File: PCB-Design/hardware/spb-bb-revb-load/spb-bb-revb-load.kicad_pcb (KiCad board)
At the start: 4 copper layers, 89.5 x 80 mm, 200 parts, among them J1 DC+, J10 U.FL L2, J11 U.FL D2, J12 V_ISO,HS in: 1 +, 2 -, J13 V_ISO,LS in: 1 +, 2 -, J14 CTRL2: 1 12V 2 GND 3 PWM_H 4 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, J15 FAN 12V: 1 +12V, 2 GND, J16 U.FL H3, J17 U.FL L3, J18 U.FL D3, J19 U.FL H4, J2 DC-, J20 U.FL L4, J21 U.FL D4, J22 AC, J23 1:NTC 2:DC- (LS domain!), J3 V_ISO,HS in: 1 +, 2 -, J4 V_ISO,LS in: 1 +, 2 -, J5 CTRL1: 1 12V 2 GND 3 PWM_H 4 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, J6 U.FL H1, J7 U.FL L1, J8 U.FL D1, J9 U.FL H2, Q1 EPC2361, Q2 EPC2361, Q3 EPC2361, Q4 EPC2361, Q5 EPC2361, Q6 EPC2361, Q7 EPC2361, Q8 EPC2361, U1 2EDF7275K, U2 2EDF7275K

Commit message: Rev B boards: full silkscreen; Q3D fast set fixed (R-only DC, bank model)
- silk_placer.py: collision-checked placement (pads, silk, outline) of every reference
  (connectors with their function, U.FL with the measured signal), connector pin names, DC+/DC-,
  AC, cell numbers, polarity warning, board name; DRC 0/0/0 on both boards; fab files regenerated
- Q3D: DC solved for R only (the DC-inductance pass hung > 19 h), new bank crop (terminals +
  bank + bypass, AC 1 MHz) for the leg DC-link port and L_b; final_post after every step

Co-Authored-By: Claude Opus 5.5 <noreply@anthropic.com>
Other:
- board text added: "+"
- board text added: "+12V"
- board text added: "-"
- board text added: "12V"
- board text added: "2"
- board text added: "3"
- board text added: "75 V DC - CHECK POLARITY"
- board text added: "AC"
- board text added: "C1"
- board text added: "C10"
- board text added: "C11"
- board text added: "C12"
- board text added: "C13"
- board text added: "C14"
- board text added: "C15"
- board text added: "C16"
- board text added: "C17"
- board text added: "C18"
- board text added: "C19"
- board text added: "C2"
- board text added: "C20"
- board text added: "C21"
- board text added: "C22"
- board text added: "C23"
- board text added: "C24"
- board text added: "C25"
- board text added: "C26"
- board text added: "C27"
- board text added: "C28"
- board text added: "C29"
- board text added: "C3"
- board text added: "C30"
- board text added: "C31"
- board text added: "C32"
- board text added: "C33"
- board text added: "C34"
- board text added: "C35"
- board text added: "C36"
- board text added: "C37"
- board text added: "C38"
- board text added: "C39"
- board text added: "C4"
- board text added: "C40"
- board text added: "C41"
- board text added: "C42"
- board text added: "C43"
- board text added: "C44"
- board text added: "C45"
- board text added: "C46"
- board text added: "C47"
- board text added: "C48"
- board text added: "C49"
- board text added: "C5"
- board text added: "C50"
- board text added: "C51"
- board text added: "C52"
- board text added: "C53"
- board text added: "C54"
- board text added: "C55"
- board text added: "C56"
- board text added: "C57"
- board text added: "C58"
- board text added: "C59"
- board text added: "C6"
- board text added: "C60"
- board text added: "C61"
- board text added: "C62"
- board text added: "C63"
- board text added: "C64"
- board text added: "C65"
- board text added: "C66"
- board text added: "C67"
- board text added: "C68"
- board text added: "C69"
- board text added: "C7"
- board text added: "C70"
- board text added: "C71"
- board text added: "C72"
- board text added: "C73"
- board text added: "C74"
- board text added: "C75"
- board text added: "C76"
- board text added: "C77"
- board text added: "C78"
- board text added: "C79"
- board text added: "C8"
- board text added: "C80"
- board text added: "C81"
- board text added: "C82"
- board text added: "C83"
- board text added: "C84"
- board text added: "C85"
- board text added: "C86"
- board text added: "C87"
- board text added: "C88"
- board text added: "C9"
- board text added: "CELL 1"
- board text added: "CELL 4"
- board text added: "D1"
- board text added: "D10 HV"
- board text added: "D2"
- board text added: "D3"
- board text added: "D4"
- board text added: "D5 12V"
- board text added: "D6"
- board text added: "D7"
- board text added: "D8"
- board text added: "D9"
- board text added: "DIS"
- board text added: "GND"
- board text added: "J1 DC+"
- board text added: "J10 VGS-L2"
- board text added: "J11 VDS-L2"
- board text added: "J12 HS-ISO"
- board text added: "J13 LS-ISO"
- board text added: "J14 CTRL2"
- board text added: "J15 FAN"
- board text added: "J16 VGS-H3"
- board text added: "J17 VGS-L3"
- board text added: "J18 VDS-L3"
- board text added: "J19 VGS-H4"
- board text added: "J2 DC-"
- board text added: "J20 VGS-L4"
- board text added: "J21 VDS-L4"
- board text added: "J22 AC"
- board text added: "J23 NTC"
- board text added: "J3 HS-ISO"
- board text added: "J4 LS-ISO"
- board text added: "J5 CTRL1"
- board text added: "J6 VGS-H1"
- board text added: "J7 VGS-L1"
- board text added: "J8 VDS-L1"
- board text added: "J9 VGS-H2"
- board text added: "KTH 2026-10 4 x EPC2361 PER SWITCH"
- board text added: "L1"
- board text added: "L10"
- board text added: "L2"
- board text added: "L3"
- board text added: "L4"
- board text added: "L5"
- board text added: "L6"
- board text added: "L7"
- board text added: "L8"
- board text added: "L9"
- board text added: "NTC"
- board text added: "PWMH"
- board text added: "PWML"
- board text added: "Q1"
- board text added: "Q2"
- board text added: "Q3"
- board text added: "Q4"
- board text added: "Q5"
- board text added: "Q6"
- board text added: "Q7"
- board text added: "Q8"
- board text added: "R1"
- board text added: "R10"
- board text added: "R11"
- board text added: "R12"
- board text added: "R13"
- board text added: "R14"
- board text added: "R15"
- board text added: "R16"
- board text added: "R17"
- board text added: "R18"
- board text added: "R19"
- board text added: "R2"
- board text added: "R20"
- board text added: "R21"
- board text added: "R22"
- board text added: "R23"
- board text added: "R24"
- board text added: "R25"
- board text added: "R26"
- board text added: "R27"
- board text added: "R28"
- board text added: "R29"
- board text added: "R3"
- board text added: "R30"
- board text added: "R31"
- board text added: "R32"
- board text added: "R33"
- board text added: "R34"
- board text added: "R35"
- board text added: "R36"
- board text added: "R37"
- board text added: "R38"
- board text added: "R39"
- board text added: "R4"
- board text added: "R40"
- board text added: "R41"
- board text added: "R42"
- board text added: "R43"
- board text added: "R44"
- board text added: "R45"
- board text added: "R46"
- board text added: "R47"
- board text added: "R48"
- board text added: "R49"
- board text added: "R5"
- board text added: "R50"
- board text added: "R6"
- board text added: "R7"
- board text added: "R8"
- board text added: "R9"
- board text added: "RT1"
- board text added: "SPB LEG REV B - LOAD-TEST BOARD"
- board text added: "U1"
- board text added: "U2"
- board text removed: "HV"

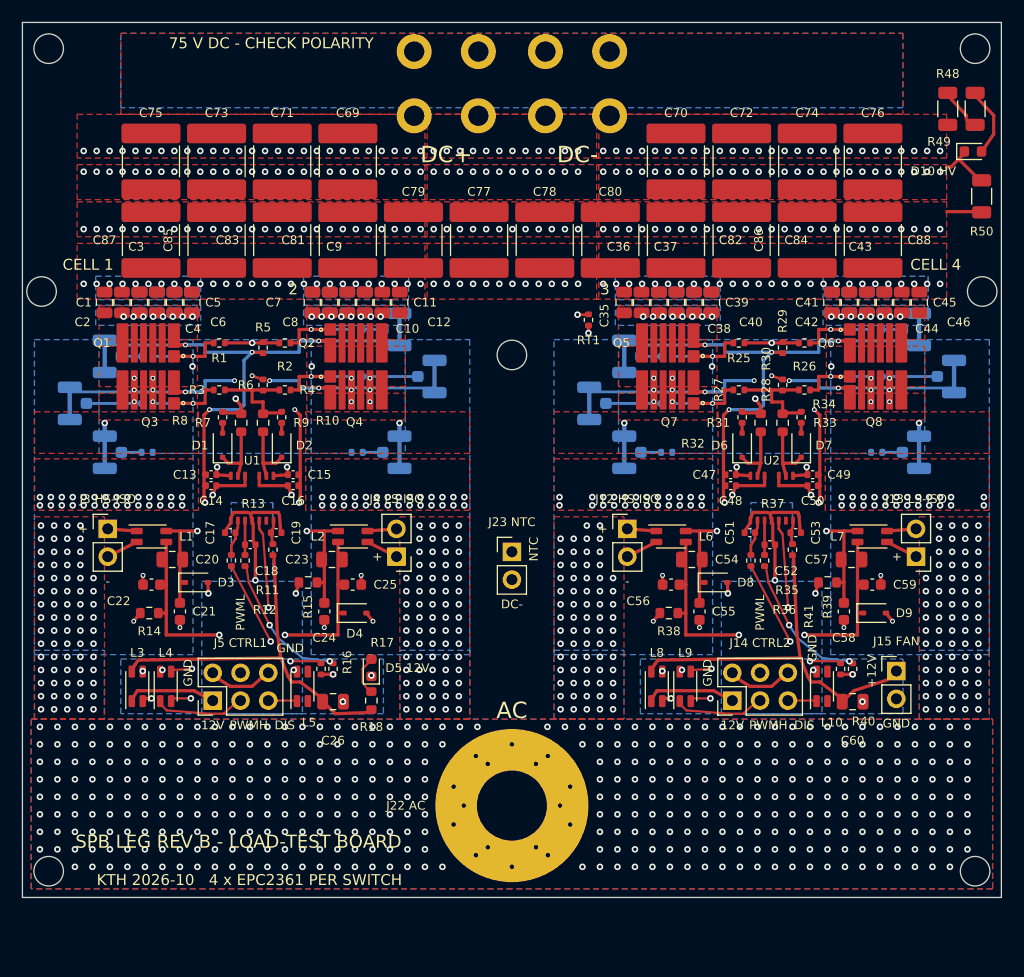
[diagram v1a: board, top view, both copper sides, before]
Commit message: Rev B boards: 1200 V control/power barrier and per-pair common-mode filtering
- Rule set in <board>.kicad_dru (exact net lists): control vs power 4.0 mm on the outer
  layers (IPC-2221B B4/A6), 3.0 mm inner (B1), 3.0 mm inside the 2EDF7275K courtyard,
  0.2 mm between the 75 V power domains. DRC 0/0 on both boards, schematic = PCB.
- Control area per block: top-layer SMD only (+ bottom GNDI plane), 4 mm / 3 mm barrier
  keepouts, nothing under the chokes and the connector on any layer.
- 2x5 SMT control header with a return next to every signal (PWM_H, PWM_L, DIS, 12 V,
  NTC), one WE-CNSW choke per pair, 12 V ferrite bead; NTC moved to the control side.
- Gate-supply islands moved outside the barrier, supplies routed on L3 around it,
  output decoupling on the bottom; AC bus/bolt 5.2 mm lower (board 89.5 x 85.2 mm).
- Removed: DC- referenced NTC header, 12 V LED, fan header (fan from the bench).
- Fab notes: IPC class 2, solder mask over all copper, all vias tented.

Co-Authored-By: Claude Opus 5.5 <noreply@anthropic.com>
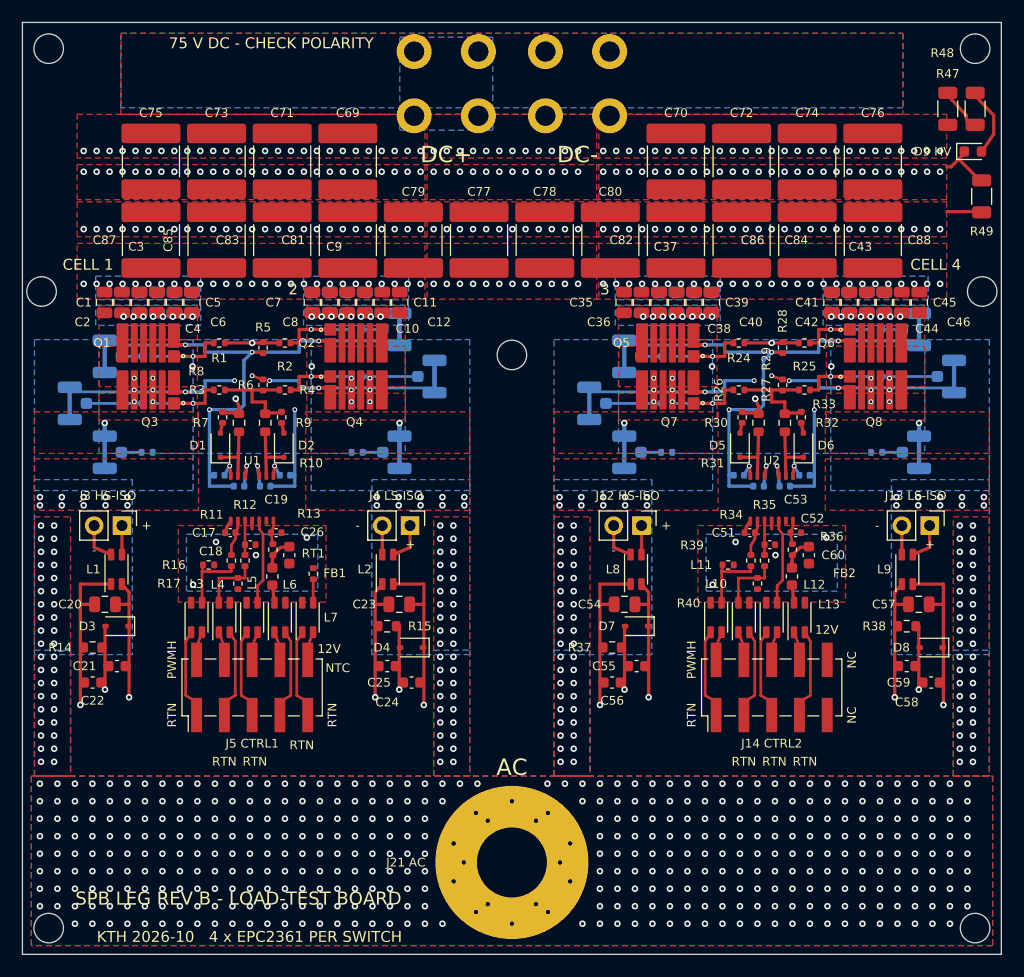
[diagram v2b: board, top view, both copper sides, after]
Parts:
- removed D10: red 0603 (DC link present), LED_SMD:LED_0603_1608Metric
- removed J22: AC, spb_fab:AC_BOLT_M6
- removed J23: 1:NTC 2:DC- (LS domain!), Connector_PinHeader_2.54mm:PinHeader_1x02_P2.54mm_Vertical
- removed R50: 100k 1206 (bleeder), Resistor_SMD:R_1206_3216Metric
- added FB1: BLM18PG221SN1 (220 R @ 100 MHz), Inductor_SMD:L_0603_1608Metric, F.Cu at (128.1, 126.2)
- added FB2: BLM18PG221SN1 (220 R @ 100 MHz), Inductor_SMD:L_0603_1608Metric, F.Cu at (175.6, 126.2)
- added L11: WE-CNSW 744232601, spb_fab:L_CommonMode_Wurth_WE-CNSW-1206, F.Cu at (171.2, 130.0)
- added L12: WE-CNSW 744232601, spb_fab:L_CommonMode_Wurth_WE-CNSW-1206, F.Cu at (173.8, 130.0)
- added L13: WE-CNSW 744232601, spb_fab:L_CommonMode_Wurth_WE-CNSW-1206, F.Cu at (176.3, 130.0)
- C13, C14, C15, C16, C47, C48, C49, C50: moved to B.Cu
- C26, C60: value 4.7uF 25V X7R 0805 (12 V) -> 4.7uF 25V X5R 0603 (12 V); footprint Capacitor_SMD:C_0805_2012Metric -> Capacitor_SMD:C_0603_1608Metric
- D5: value green 0603 (12 V) -> PMEG3020EJ; footprint LED_SMD:LED_0603_1608Metric -> Diode_SMD:D_SOD-323F
- D7: value PMEG3020EJ -> BZX384-C5V1; footprint Diode_SMD:D_SOD-323F -> Diode_SMD:D_SOD-323
- D9: value BZX384-C5V1 -> red 0603 (DC link present); footprint Diode_SMD:D_SOD-323 -> LED_SMD:LED_0603_1608Metric
- J14: value CTRL2: 1 12V 2 GND 3 PWM_H 4 PWM_L 5 DIS 6 GND -> CTRL2: 1 RTN 2 PWMH 3 RTN 4 PWML 5 RTN 6 DIS 7 RTN 8 12V 9 NC 10 NC; footprint Connector_PinHeader_2.54mm:PinHeader_2x03_P2.54mm_Vertical -> spb_fab:PinHeader_2x05_P2.54mm_Vertical_SMD
- J15: value FAN 12V: 1 +12V, 2 GND -> U.FL H3; footprint Connector_PinHeader_2.54mm:PinHeader_1x02_P2.54mm_Vertical -> spb_fab:U.FL_Hirose_U.FL-R-SMT-1_Vertical; moved to B.Cu
- J16: value U.FL H3 -> U.FL L3
- J17: value U.FL L3 -> U.FL D3
- J18: value U.FL D3 -> U.FL H4
- J19: value U.FL H4 -> U.FL L4
- J20: value U.FL L4 -> U.FL D4
- J21: value U.FL D4 -> AC; footprint spb_fab:U.FL_Hirose_U.FL-R-SMT-1_Vertical -> spb_fab:AC_BOLT_M6; moved to F.Cu
- J5: value CTRL1: 1 12V 2 GND 3 PWM_H 4 PWM_L 5 DIS 6 GND -> CTRL1: 1 RTN 2 PWMH 3 RTN 4 PWML 5 RTN 6 DIS 7 RTN 8 12V 9 RTN 10 NTC; footprint Connector_PinHeader_2.54mm:PinHeader_2x03_P2.54mm_Vertical -> spb_fab:PinHeader_2x05_P2.54mm_Vertical_SMD
- R18: value 4.7k (LED) -> 0R (V_GS HS); footprint Resistor_SMD:R_0603_1608Metric -> Resistor_SMD:R_0402_1005Metric; moved to B.Cu
- R19, R22, R42, R45: value 0R (V_GS HS) -> 0R (V_GS LS)
- R20, R23, R43, R46: value 0R (V_GS LS) -> 953R 1% (V_DS LS, 20:1 into 50 R)
- R21, R44: value 953R 1% (V_DS LS, 20:1 into 50 R) -> 0R (V_GS HS)
- R24: value 953R 1% (V_DS LS, 20:1 into 50 R) -> 0R5 1% (R_G HL); moved to F.Cu
- R25: value 0R5 1% (R_G HL) -> 0R5 1% (R_G HR)
- R26: value 0R5 1% (R_G HR) -> 0R5 1% (R_G LL)
- R27: value 0R5 1% (R_G LL) -> 0R5 1% (R_G LR)
- R28: value 0R5 1% (R_G LR) -> 10k 1% (HS gate pull-down)
- R29: value 10k 1% (HS gate pull-down) -> 10k 1% (LS gate pull-down)
- R30: value 10k 1% (LS gate pull-down) -> 0R75 1% (R_ON,A); footprint Resistor_SMD:R_0402_1005Metric -> Resistor_SMD:R_0603_1608Metric
- R31: value 0R75 1% (R_ON,A) -> 0R (R_OFF,A); footprint Resistor_SMD:R_0603_1608Metric -> Resistor_SMD:R_0402_1005Metric
- R32: value 0R (R_OFF,A) -> 0R75 1% (R_ON,B); footprint Resistor_SMD:R_0402_1005Metric -> Resistor_SMD:R_0603_1608Metric
- R33: value 0R75 1% (R_ON,B) -> 0R (R_OFF,B); footprint Resistor_SMD:R_0603_1608Metric -> Resistor_SMD:R_0402_1005Metric
- R34: value 0R (R_OFF,B) -> 47R 1% (INA)
- R35: value 47R 1% (INA) -> 47R 1% (INB)
- R36: value 47R 1% (INB) -> 3k 1% (RVDDI)
- R37: value 3k 1% (RVDDI) -> 150R 1% 0603 (bias, <= 82 mW); footprint Resistor_SMD:R_0402_1005Metric -> Resistor_SMD:R_0603_1608Metric
- R39: value 150R 1% 0603 (bias, <= 82 mW) -> 10k (PWM_H pull-down); footprint Resistor_SMD:R_0603_1608Metric -> Resistor_SMD:R_0402_1005Metric
- R40: value 10k (PWM_H pull-down) -> 10k (PWM_L pull-down)
- R41: value 10k (PWM_L pull-down) -> 0R (V_GS HS); moved to B.Cu
- R47: value 953R 1% (V_DS LS, 20:1 into 50 R) -> 68k 1206 (HV LED); footprint Resistor_SMD:R_0402_1005Metric -> Resistor_SMD:R_1206_3216Metric; moved to F.Cu
- R49: value 68k 1206 (HV LED) -> 100k 1206 (bleeder)
- moved J21 52.5 mm to (150.0, 152.4)
- moved L7 52.1 mm to (131.3, 130.0), turned to 90 degrees
- moved D9 43.1 mm to (192.2, 87.4)
- moved D5 39.4 mm to (170.8, 114.2)
- moved J15 37.7 mm to (160.8, 106.1), turned to 180 degrees
- moved R18 37.6 mm to (116.7, 106.1), turned to 0 degrees
- moved L6 36.5 mm to (128.8, 130.0), turned to 90 degrees
- moved R24 36.3 mm to (170.8, 104.9)
- moved RT1 34.2 mm to (131.8, 126.0)
- moved R41 33.2 mm to (164.2, 106.1), turned to 0 degrees
- moved R47 32.1 mm to (189.8, 83.5), turned to 90 degrees
- moved J18 28.3 mm to (186.8, 103.7), turned to 0 degrees
- moved L9 22.9 mm to (186.2, 125.6)
- moved D7 22.4 mm to (161.4, 130.8), turned to 180 degrees
- moved R21 22.2 mm to (135.8, 103.7)
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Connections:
- C22 pad 1: KH1 -> VEEA1
- C22 pad 2: VEEA1 -> KH1
- C24 pad 1: KL1 -> VEEB1
- C24 pad 2: VEEB1 -> KL1
- C25 pad 1: VDDB1 -> KL1
- C25 pad 2: KL1 -> VDDB1
- C26 pad 1: +12V1 -> GNDI1
- C26 pad 2: GNDI1 -> +12V1
- C56 pad 1: KH2 -> VEEA2
- C56 pad 2: VEEA2 -> KH2
- C58 pad 1: KL2 -> VEEB2
- C58 pad 2: VEEB2 -> KL2
- C59 pad 1: VDDB2 -> KL2
- C59 pad 2: KL2 -> VDDB2
- C60 pad 1: +12V2 -> GNDI2
- C60 pad 2: GNDI2 -> +12V2
- D5 pad 1: GNDI1 -> OUTA2
- D5 pad 2: LEDA_12V1 -> OFFA2
- D6 pad 1: OUTA2 -> OUTB2
- D6 pad 2: OFFA2 -> OFFB2
- D7 pad 1: OUTB2 -> VDDA2
- D7 pad 2: OFFB2 -> KH2
- D8 pad 1: VDDA2 -> VDDB2
- D8 pad 2: KH2 -> KL2
- D9 pad 1: VDDB2 -> DCN
- D9 pad 2: KL2 -> HVB
- J14 pad 1: C_12V2 -> C_RTN_PWMH2
- J14 pad 2: C_GND2 -> C_PWMH2
- J14 pad 3: C_PWMH2 -> C_RTN_PWML2
- J14 pad 5: C_DIS2 -> C_RTN_DIS2
- J14 pad 6: C_GND2 -> C_DIS2
- J15 pad 1: +12V2 -> UFL_H3
- J15 pad 2: GNDI2 -> KH2
- J16 pad 1: UFL_H3 -> UFL_L3
- J16 pad 2: KH2 -> KL2
- J17 pad 1: UFL_L3 -> UFL_D3
- J17 pad 2: KL2 -> DCN
- J18 pad 1: UFL_D3 -> UFL_H4
- J18 pad 2: DCN -> KH2
- J19 pad 1: UFL_H4 -> UFL_L4
- J19 pad 2: KH2 -> KL2
- J20 pad 1: UFL_L4 -> UFL_D4
- J20 pad 2: KL2 -> DCN
- J21 pad 1: UFL_D4 -> SW
- J5 pad 1: C_12V1 -> C_RTN_PWMH1
- J5 pad 2: C_GND1 -> C_PWMH1
- J5 pad 3: C_PWMH1 -> C_RTN_PWML1
- J5 pad 5: C_DIS1 -> C_RTN_DIS1
- J5 pad 6: C_GND1 -> C_DIS1
- L1 pad 1: VINA_P1 -> VEEA1
- L1 pad 2: VDDA1 -> VINA_N1
- L1 pad 3: VEEA1 -> VINA_P1
- L1 pad 4: VINA_N1 -> VDDA1
- L10 pad 1: C_DIS2 -> C_RTN_PWMH2
- L10 pad 2: DIS2 -> GNDI2
- L10 pad 3: (no net) -> PWM_H2
- L10 pad 4: (no net) -> C_PWMH2
- L3 pad 1: C_12V1 -> C_RTN_PWMH1
- L3 pad 2: +12V1 -> GNDI1
- L3 pad 3: GNDI1 -> PWM_H1
- L3 pad 4: C_GND1 -> C_PWMH1
- L4 pad 1: C_PWMH1 -> C_PWML1
- L4 pad 2: PWM_H1 -> PWM_L1
- L4 pad 3: PWM_L1 -> GNDI1
- L4 pad 4: C_PWML1 -> C_RTN_PWML1
- L5 pad 1: C_DIS1 -> C_RTN_DIS1
- L5 pad 2: DIS1 -> GNDI1
- L5 pad 3: (no net) -> DIS1
- L5 pad 4: (no net) -> C_DIS1
- L6 pad 1: VINA_P2 -> C_12V1
- L6 pad 2: VDDA2 -> 12V_CM1
- L6 pad 3: VEEA2 -> GNDI1
- L6 pad 4: VINA_N2 -> C_RTN_12V1
- L7 pad 1: VEEB2 -> C_RTN_NTC1
- L7 pad 2: VINB_N2 -> GNDI1
- L7 pad 3: VINB_P2 -> NTC
- L7 pad 4: VDDB2 -> C_NTC1
- L8 pad 1: C_12V2 -> VEEA2
- L8 pad 2: +12V2 -> VINA_N2
- L8 pad 3: GNDI2 -> VINA_P2
- L8 pad 4: C_GND2 -> VDDA2
- L9 pad 1: C_PWMH2 -> VEEB2
- L9 pad 2: PWM_H2 -> VINB_N2
- L9 pad 3: PWM_L2 -> VINB_P2
- L9 pad 4: C_PWML2 -> VDDB2
- R14 pad 1: KH1 -> VEEA1
- R14 pad 2: VEEA1 -> KH1
- R15 pad 1: KL1 -> VEEB1
- R15 pad 2: VEEB1 -> KL1
- R16 pad 1: GNDI1 -> PWM_H1
- R16 pad 2: PWM_H1 -> GNDI1
- R18 pad 1: +12V1 -> UFL_H1
- R18 pad 2: LEDA_12V1 -> GH_L1
- R19 pad 1: UFL_H1 -> UFL_L1
- R19 pad 2: GH_L1 -> GL_L1
- R20 pad 1: UFL_L1 -> UFL_D1
- R20 pad 2: GL_L1 -> SW
- R21 pad 1: UFL_D1 -> GH_R1
- R21 pad 2: SW -> UFL_H2
- R22 pad 1: GH_R1 -> GL_R1
- R22 pad 2: UFL_H2 -> UFL_L2
- R23 pad 1: GL_R1 -> SW
- R23 pad 2: UFL_L2 -> UFL_D2
- R24 pad 1: SW -> GH_L2
- R24 pad 2: UFL_D2 -> GH_STAR2
- R25 pad 1: GH_L2 -> GH_STAR2
- R25 pad 2: GH_STAR2 -> GH_R2
- R26 pad 1: GH_STAR2 -> GL_L2
- R26 pad 2: GH_R2 -> GL_STAR2
- R27 pad 1: GL_L2 -> GL_STAR2
- R27 pad 2: GL_STAR2 -> GL_R2
- R28 pad 1: GL_STAR2 -> KH2
- R28 pad 2: GL_R2 -> GH_STAR2
- R29 pad 1: KH2 -> GL_STAR2
- R29 pad 2: GH_STAR2 -> KL2
- R30 pad 1: GL_STAR2 -> OUTA2
- R30 pad 2: KL2 -> GH_STAR2
- R31 pad 1: OUTA2 -> OFFA2
- R32 pad 1: OFFA2 -> OUTB2
- R32 pad 2: GH_STAR2 -> GL_STAR2
- R33 pad 1: OUTB2 -> OFFB2
- R34 pad 1: OFFB2 -> PWM_H2
- R34 pad 2: GL_STAR2 -> INA2
- R35 pad 1: PWM_H2 -> PWM_L2
- R35 pad 2: INA2 -> INB2
- R36 pad 1: PWM_L2 -> +12V2
- R36 pad 2: INB2 -> VDDI2
- R37 pad 1: +12V2 -> VEEA2
- R37 pad 2: VDDI2 -> KH2
- R38 pad 1: KH2 -> VEEB2
- R38 pad 2: VEEA2 -> KL2
- R39 pad 1: KL2 -> PWM_H2
- R39 pad 2: VEEB2 -> GNDI2
- R40 pad 2: PWM_H2 -> PWM_L2
- R41 pad 1: GNDI2 -> UFL_H3
- R41 pad 2: PWM_L2 -> GH_L2
- R42 pad 1: UFL_H3 -> UFL_L3
- R42 pad 2: GH_L2 -> GL_L2
- R43 pad 1: UFL_L3 -> UFL_D3
- R43 pad 2: GL_L2 -> SW
- R44 pad 1: UFL_D3 -> GH_R2
- R44 pad 2: SW -> UFL_H4
- R45 pad 1: GH_R2 -> GL_R2
- R45 pad 2: UFL_H4 -> UFL_L4
- R46 pad 1: GL_R2 -> SW
- R46 pad 2: UFL_L4 -> UFL_D4
- R47 pad 1: SW -> DCP
- R47 pad 2: UFL_D4 -> HVA
- R48 pad 1: DCP -> HVA
- R48 pad 2: HVA -> HVB
- R49 pad 1: HVA -> DCP
- R49 pad 2: HVB -> DCN
- RT1 pad 1: DCN -> NTC
- RT1 pad 2: NTC -> GNDI1
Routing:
- net KH1: track 67.1 -> 97.8 mm, vias 9 -> 5
- net KH2: track 67.1 -> 97.8 mm, vias 9 -> 5
- net KL2: track 71.9 -> 102.5 mm, vias 11 -> 7
- net KL1: track 71.9 -> 102.5 mm, vias 11 -> 7
- net +12V2: track 32.2 -> 2.96 mm
- net +12V1: track 32.0 -> 2.96 mm
- net VDDA1: track 19.5 -> 44.4 mm
- net VEEB2: track 19.7 -> 44.7 mm
- net VEEB1: track 19.7 -> 44.7 mm
- net VDDA2: track 19.5 -> 44.4 mm
- net NTC: track 26.9 -> 2.14 mm, vias 1 -> 0
- net VEEA1: track 32.1 -> 55.6 mm
- net VDDB2: track 31.9 -> 55.4 mm
- net VEEA2: track 32.1 -> 55.6 mm
- net VDDB1: track 31.9 -> 55.4 mm
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- added copper zone on F.Cu, net GNDI1
- added copper zone on F.Cu, net GNDI2
- removed copper zone on In1.Cu, net GNDI1
- removed copper zone on In1.Cu, net GNDI2
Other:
- board size 89.5 x 80 mm -> 89.5 x 85.2 mm
- board text added: "D5"
- board text added: "D9 HV"
- board text added: "FB1"
- board text added: "FB2"
- board text added: "J15 VGS-H3"
- board text added: "J16 VGS-L3"
- board text added: "J17 VDS-L3"
- board text added: "J18 VGS-H4"
- board text added: "J19 VGS-L4"
- board text added: "J20 VDS-L4"
- board text added: "J21 AC"
- board text added: "L11"
- board text added: "L12"
- board text added: "L13"
- board text added: "NC"
- board text added: "RTN"
- board text removed: "+12V"
- board text removed: "D10 HV"
- board text removed: "D5 12V"
- board text removed: "D9"
- board text removed: "DIS"
- board text removed: "GND"
- board text removed: "J15 FAN"
- board text removed: "J16 VGS-H3"
- board text removed: "J17 VGS-L3"
- board text removed: "J18 VDS-L3"
- board text removed: "J19 VGS-H4"
- board text removed: "J20 VGS-L4"
- board text removed: "J21 VDS-L4"
- board text removed: "J22 AC"
- board text removed: "J23 NTC"
- board text removed: "PWML"
- board text removed: "R50"
